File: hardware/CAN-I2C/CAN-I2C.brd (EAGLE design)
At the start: 90.2 x 15.2 mm, 31 parts, among them Q1 12MHZ, U1 MCP2515(MCP2510)ML, U2 MCP2551, U4 ATTINY816M

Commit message: Re-arranging directory structure
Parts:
- moved C2 10.2 mm to (7.62, 14.0), turned to 0 degrees
- moved R1 8.03 mm to (12.7, 1.27), turned to 180 degrees
- moved R3 7.73 mm to (2.54, 14.0), turned to 180 degrees
- moved R2 6.35 mm to (10.2, 12.7)
- moved C7 2.84 mm to (26.7, 7.62), turned to 0 degrees
- moved U4 2.84 mm to (26.7, 11.4), turned to 90 degrees
- moved C5 1.80 mm to (19.1, 2.54), turned to 0 degrees
- moved Q1 1.80 mm to (19.1, 5.08), turned to 0 degrees
- moved SPI 1.27 mm to (25.4, 3.81)
- moved C3 1.27 mm to (12.7, 8.89)
- moved C6 1.27 mm to (22.9, 5.08)
- moved U2 1.27 mm to (12.7, 5.08)
- moved C4 1.27 mm to (19.1, 12.7), turned to 0 degrees
- moved D2 1.27 mm to (12.7, 12.7)
- moved U1 1.27 mm to (19.1, 8.89)
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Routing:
- net +3V3: track 84.7 -> 0.00 mm, vias 3 -> 0
- net +5V: track 59.0 -> 0.00 mm, vias 1 -> 0
- net +12V: track 51.1 -> 0.00 mm, vias 1 -> 0
- net MISO: track 49.1 -> 0.00 mm, vias 2 -> 0
- net MOSI: track 42.9 -> 0.00 mm, vias 4 -> 0
- net SCK: track 41.5 -> 0.00 mm, vias 1 -> 0
- net !OUT_CS!: track 36.9 -> 0.00 mm, vias 1 -> 0
- net CLK: track 30.9 -> 0.00 mm, vias 2 -> 0
- net N$4: track 30.1 -> 0.00 mm, vias 3 -> 0
- net N$5: track 29.6 -> 0.00 mm, vias 1 -> 0
- net SCL: track 22.4 -> 0.00 mm, vias 1 -> 0
- net SDA: track 21.9 -> 0.00 mm, vias 1 -> 0
- net RST: track 20.2 -> 0.00 mm
- net N$2: track 13.2 -> 0.00 mm
- net N$13: track 12.4 -> 0.00 mm, vias 1 -> 0
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
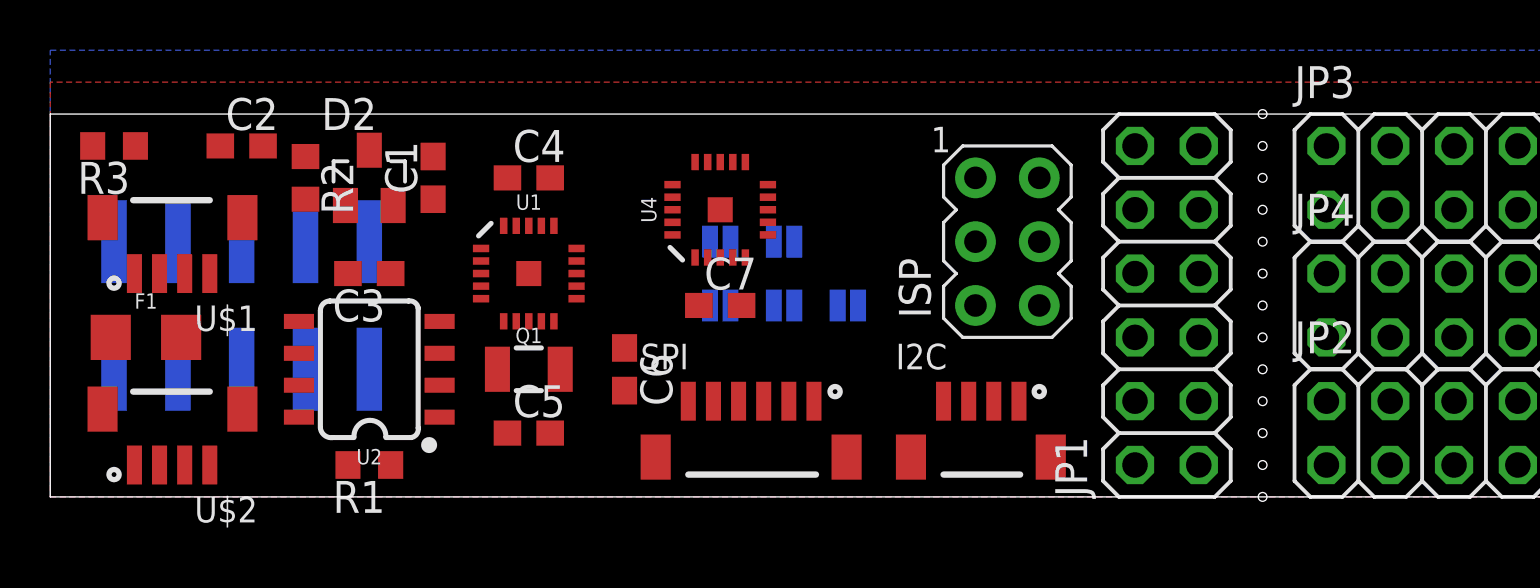
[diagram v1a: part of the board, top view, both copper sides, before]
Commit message: Silkscreen and routing cleanup
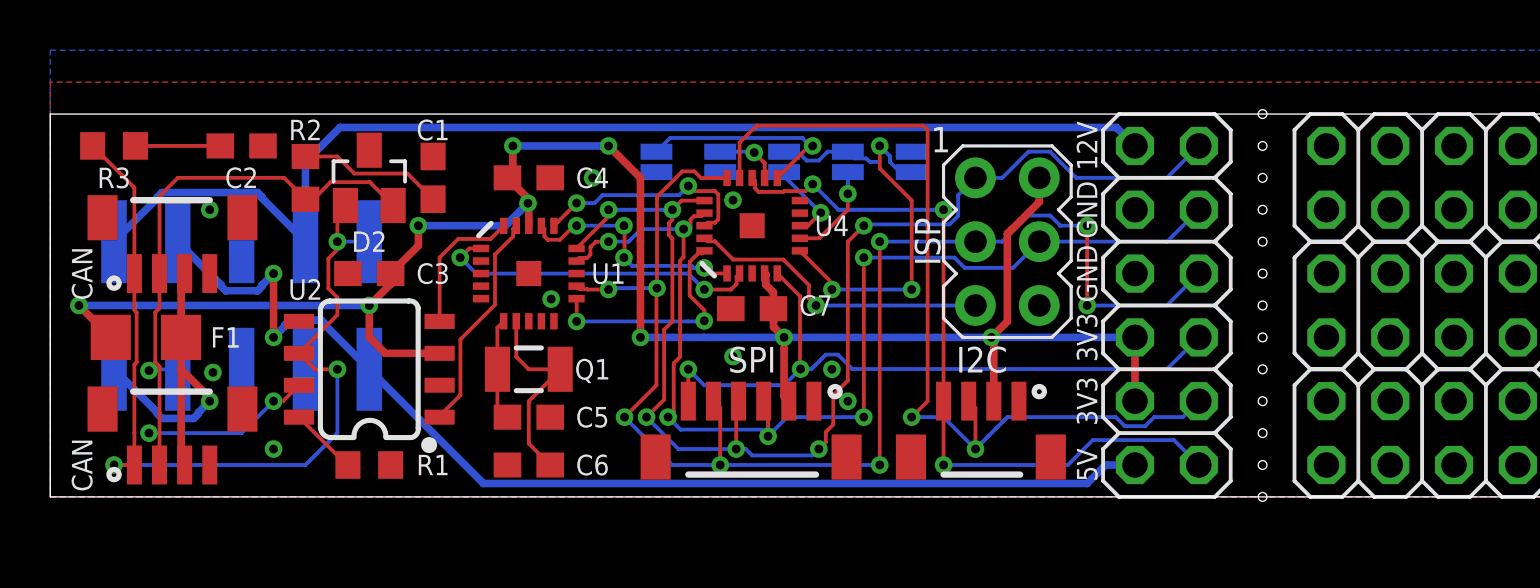
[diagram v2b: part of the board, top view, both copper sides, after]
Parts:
- moved DIR 9.53 mm to (24.1, 13.3), turned to 270 degrees
- moved AD3 9.52 mm to (34.3, 13.3), turned to 90 degrees
- moved AD0 6.25 mm to (26.7, 13.3), turned to 270 degrees
- moved AD2 5.99 mm to (31.8, 13.3), turned to 90 degrees
- moved C6 5.39 mm to (19.1, 1.27), turned to 180 degrees
- moved AD1 3.18 mm to (29.2, 13.3), turned to 90 degrees
- moved U4 1.42 mm to (27.9, 10.8)
- moved C7 1.28 mm to (27.9, 7.49), turned to 180 degrees
- moved C5 0.63 mm to (19.1, 3.17)
- renumbered CAN-RIBBON to RIBBON, U$1 to CAN-IN, U$2 to CAN-OUT
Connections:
- net !OUT_CS!: now also JP1.5; no longer JP1.11
- net +12V: now also JP1.12; no longer JP1.8
- net +3V3: now also JP1.6; no longer JP1.2
- net +5V: now also JP1.2; no longer JP1.6
- net GND: now also JP1.8; no longer JP1.12
- net MISO: now also JP1.11; no longer JP1.9
- net MOSI: now also JP1.9; no longer JP1.7
- net SCK: now also JP1.7; no longer JP1.5
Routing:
- net +3V3: track 0.00 -> 80.0 mm, vias 0 -> 9
- net SCK: track 0.00 -> 55.4 mm, vias 0 -> 8
- net MISO: track 0.00 -> 50.0 mm, vias 0 -> 6
- net +12V: track 0.00 -> 46.4 mm
- net +5V: track 0.00 -> 45.1 mm, vias 0 -> 2
- net MOSI: track 0.00 -> 44.7 mm, vias 0 -> 6
- net N$5: track 0.00 -> 36.2 mm, vias 0 -> 3
- net SCL: track 0.00 -> 36.0 mm, vias 0 -> 2
- net N$4: track 0.00 -> 30.2 mm, vias 0 -> 3
- net SDA: track 0.00 -> 29.7 mm, vias 0 -> 3
- net !OUT_CS!: track 0.00 -> 27.3 mm, vias 0 -> 2
- net N$13: track 0.00 -> 14.4 mm, vias 0 -> 1
- net N$15: track 0.00 -> 13.3 mm, vias 0 -> 3
- net CLK: track 0.00 -> 13.1 mm, vias 0 -> 2
- net RST: track 0.00 -> 12.2 mm, vias 0 -> 1
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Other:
- board text added: "!CS!"
- board text added: "+12V"
- board text added: "+3V3"
- board text added: "+5V"
- board text added: "12V"
- board text added: "3V3"
- board text added: "5V"
- board text added: "CAN"
- board text added: "CANH"
- board text added: "CANL"
- board text added: "GND"
- board text added: "MISO"
- board text added: "MOSI"
- board text added: "SCK"
- board text added: "SCL"
- board text added: "SDA"

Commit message: Added mounting tabs
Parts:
- added H1, H2: MOUNT-PAD-ROUND3.2, holes:3,2-PAD
- moved AD0 8.89 mm to (26.7, 22.2)
- moved AD1 8.89 mm to (29.2, 22.2)
- moved AD2 8.89 mm to (31.8, 22.2)
- moved AD3 8.89 mm to (34.3, 22.2)
- moved C1 8.89 mm to (15.2, 21.6)
- moved C3 8.89 mm to (12.7, 17.8)
- moved C4 8.89 mm to (19.1, 21.6)
- moved C5 8.89 mm to (19.1, 12.1)
- moved C6 8.89 mm to (19.1, 10.2)
- moved CAN-IN 8.89 mm to (3.81, 19.1)
- moved CAN-OUT 8.89 mm to (3.81, 11.4)
- moved D2 8.89 mm to (12.7, 21.6)
- moved DIR 8.89 mm to (24.1, 22.2)
- moved F1 8.89 mm to (3.81, 15.2)
- moved I2C 8.89 mm to (38.1, 11.4)
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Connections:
- net GND: now also H1.B3,2, H2.B3,2
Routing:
- net GND: vias 9 -> 11
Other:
- board size 90.2 x 15.2 mm -> 90.2 x 33 mm
